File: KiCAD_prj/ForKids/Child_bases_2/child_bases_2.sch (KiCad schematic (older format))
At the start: 61 parts, among them Q1 PN2222A, Q10 PN2222A, Q11 PN2222A, Q2 PN2222A, Q3 PN2222A, Q4 PN2222A, Q5 PN2222A, Q6 2N3904*, Q7 PN2222A, Q8 PN2222A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

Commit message: Update child_babes_2
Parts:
- R8: value 10K -> 47K
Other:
- note removed: "* можно заменить на 2222"
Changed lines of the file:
@@
 P 4650 3700
 F 0 "R8" V 4550 3700 50  0000 C CNN
-F 1 "10K" V 4750 3700 50  0000 C CNN
+F 1 "47K" V 4750 3700 50  0000 C CNN
 F 2 "" V 4580 3700 50  0001 C CNN
 F 3 "~" H 4650 3700 50  0001 C CNN
@@
 	4400 3200 4400 3350
 Connection ~ 4400 3350
-Text Notes 4450 4650 0    50   ~ 0
-* можно заменить на 2222
 $Comp
 L Device:Speaker LS2

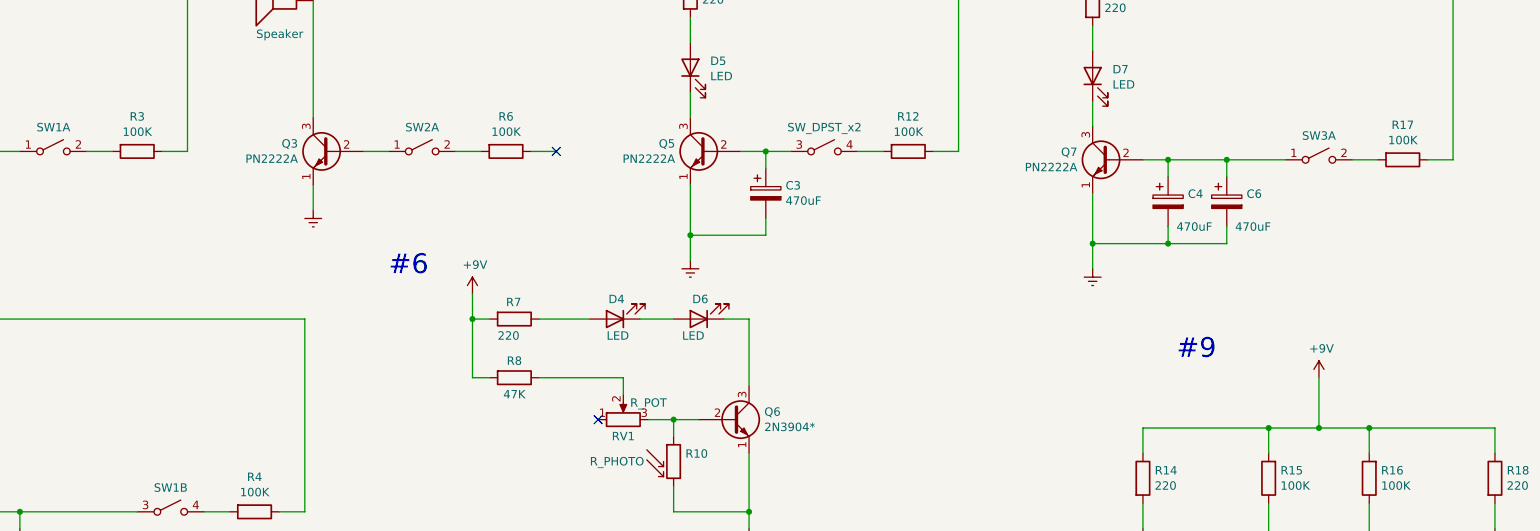
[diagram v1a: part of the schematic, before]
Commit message: Update Child Bases 2 project
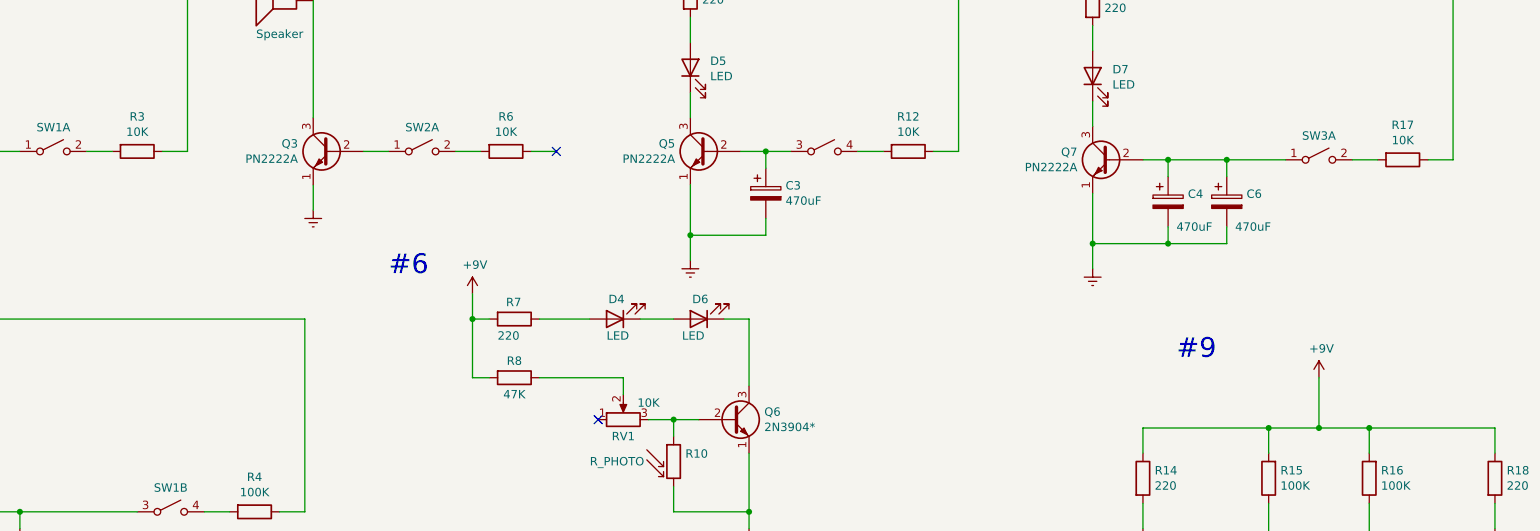
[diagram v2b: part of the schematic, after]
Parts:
- R12, R17, R3, R6: value 100K -> 10K
- RV1: value R_POT -> 10K
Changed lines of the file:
@@
 P 2400 2350
 F 0 "R3" V 2193 2350 50  0000 C CNN
-F 1 "100K" V 2284 2350 50  0000 C CNN
+F 1 "10K" V 2284 2350 50  0000 C CNN
 F 2 "" V 2330 2350 50  0001 C CNN
 F 3 "~" H 2400 2350 50  0001 C CNN
@@
 P 4600 2350
 F 0 "R6" V 4393 2350 50  0000 C CNN
-F 1 "100K" V 4484 2350 50  0000 C CNN
+F 1 "10K" V 4484 2350 50  0000 C CNN
 F 2 "" V 4530 2350 50  0001 C CNN
 F 3 "~" H 4600 2350 50  0001 C CNN
@@
 P 6500 2350
 F 0 "SW2" H 6500 2585 50  0001 C CNN
-F 1 "SW_DPST_x2" H 6500 2493 50  0000 C CNN
+F 1 "SW_DPST_x2" H 6500 2493 50  0001 C CNN
 F 2 "" H 6500 2350 50  0001 C CNN
 F 3 "~" H 6500 2350 50  0001 C CNN
@@
 P 7000 2350
 F 0 "R12" V 6793 2350 50  0000 C CNN
-F 1 "100K" V 6884 2350 50  0000 C CNN
+F 1 "10K" V 6884 2350 50  0000 C CNN
 F 2 "" V 6930 2350 50  0001 C CNN
 F 3 "~" H 7000 2350 50  0001 C CNN
@@
 P 9950 2400
 F 0 "R17" V 9743 2400 50  0000 C CNN
-F 1 "100K" V 9834 2400 50  0000 C CNN
+F 1 "10K" V 9834 2400 50  0000 C CNN
 F 2 "" V 9880 2400 50  0001 C CNN
 F 3 "~" H 9950 2400 50  0001 C CNN
@@
 P 5300 3950
 F 0 "RV1" V 5200 3950 50  0000 C CNN
-F 1 "R_POT" V 5400 3800 50  0000 C CNN
+F 1 "10K" V 5400 3800 50  0000 C CNN
 F 2 "" H 5300 3950 50  0001 C CNN
 F 3 "~" H 5300 3950 50  0001 C CNN

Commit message: Update KiCad child bases 2 project
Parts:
- R15, R16, R4: value 100K -> 10K
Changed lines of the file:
@@
 P 3100 4500
 F 0 "R4" V 2893 4500 50  0000 C CNN
-F 1 "100K" V 2984 4500 50  0000 C CNN
+F 1 "10K" V 2984 4500 50  0000 C CNN
 F 2 "" V 3030 4500 50  0001 C CNN
 F 3 "~" H 3100 4500 50  0001 C CNN
@@
 P 9150 4300
 F 0 "R15" H 9080 4254 50  0000 R CNN
-F 1 "100K" H 9080 4345 50  0000 R CNN
+F 1 "10K" H 9080 4345 50  0000 R CNN
 F 2 "" V 9080 4300 50  0001 C CNN
 F 3 "~" H 9150 4300 50  0001 C CNN
@@
 P 9750 4300
 F 0 "R16" H 9680 4254 50  0000 R CNN
-F 1 "100K" H 9680 4345 50  0000 R CNN
+F 1 "10K" H 9680 4345 50  0000 R CNN
 F 2 "" V 9680 4300 50  0001 C CNN
 F 3 "~" H 9750 4300 50  0001 C CNN
@@
 Text Notes 2700 5100 0    118  ~ 0
 #7
-Text Notes 8600 3600 0    118  ~ 0
+Text Notes 8450 6400 0    118  ~ 0
 #9
 Text Notes 1400 7400 0    118  ~ 0

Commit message: Update Child bases2 project
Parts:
- removed unit 1 of SW2
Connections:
- net at Q3.2 (B): now also R6.2
- no-connect marks 5 -> 3
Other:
- moved on the sheet: LS1
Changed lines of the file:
@@
 L Device:Speaker LS1
 U 1 1 5F978E6E
-P 3250 1350
-F 0 "LS1" H 3300 1550 50  0000 C CNN
-F 1 "Speaker" H 3250 1050 50  0000 C CNN
-F 2 "" H 3250 1150 50  0001 C CNN
-F 3 "~" H 3240 1300 50  0001 C CNN
-	1    3250 1350
+P 3250 1700
+F 0 "LS1" H 3300 1900 50  0000 C CNN
+F 1 "Speaker" H 3250 1400 50  0000 C CNN
+F 2 "" H 3250 1500 50  0001 C CNN
+F 3 "~" H 3240 1650 50  0001 C CNN
+	1    3250 1700
 	-1   0    0    -1
-$EndComp
-$Comp
-L Switch:SW_DPST_x2 SW2
-U 1 1 5F97A5C2
-P 4100 2350
-F 0 "SW2" H 4100 2493 50  0000 C CNN
-F 1 "SW_DPST_x2" H 4100 2494 50  0001 C CNN
-F 2 "" H 4100 2350 50  0001 C CNN
-F 3 "~" H 4100 2350 50  0001 C CNN
-	1    4100 2350
-	1    0    0    -1
 $EndComp
 $Comp
@@
 	3450 2700 3450 2550
 Wire Wire Line
-	3750 2350 3900 2350
-Wire Wire Line
-	4300 2350 4450 2350
-Wire Wire Line
 	4900 2350 4750 2350
-Wire Wire Line
-	3450 1450 3450 2150
 $Comp
 L power:+9V #PWR05
@@
 	1    0    0    -1
 $EndComp
-Wire Wire Line
-	2800 7000 2800 7150
-Wire Wire Line
-	2200 6800 2200 7150
-Connection ~ 2200 6800
-NoConn ~ 2200 7150
-Wire Wire Line
-	2800 7150 2550 7150
-Connection ~ 2800 7150
-Wire Wire Line
-	2800 7150 2800 7350
-NoConn ~ 2550 7150
 Text Notes 850  900  0    118  ~ 0
 #1
@@
 	3450 1250 4900 1250
 Connection ~ 3450 1250
-Wire Wire Line
-	3450 1250 3450 1350
 NoConn ~ 4900 1250
 $Comp
@@
 Wire Wire Line
 	5950 6700 5800 6700
+Wire Wire Line
+	3750 2350 4450 2350
+Wire Wire Line
+	3450 1250 3450 1700
+Wire Wire Line
+	3450 1800 3450 2150
+Wire Wire Line
+	2800 7000 2800 7350
+Wire Notes Line
+	2200 6800 2200 7150
+Wire Notes Line
+	2200 7150 2800 7150
 $EndSCHEMATC

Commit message: Update Child bases2  chem project
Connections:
- net +9V: now also R6.1
- net at LS1.2: no longer Q3.3 (C)
- no-connect marks 3 -> 1
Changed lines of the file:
@@
 	1250 1200 1250 1250
-$Comp
-L Device:Speaker LS1
-U 1 1 5F978E6E
-P 3250 1700
-F 0 "LS1" H 3300 1900 50  0000 C CNN
-F 1 "Speaker" H 3250 1400 50  0000 C CNN
-F 2 "" H 3250 1500 50  0001 C CNN
-F 3 "~" H 3240 1650 50  0001 C CNN
-	1    3250 1700
-	-1   0    0    -1
-$EndComp
 $Comp
 L Transistor_BJT:PN2222A Q3
@@
 	1    0    0    -1
 $EndComp
-NoConn ~ 4900 2350
 $Comp
 L Switch:SW_DPST_x2 SW2
@@
 Wire Wire Line
 	3450 1250 4900 1250
-Connection ~ 3450 1250
-NoConn ~ 4900 1250
 $Comp
 L Transistor_BJT:PN2222A Q10
@@
 	3750 2350 4450 2350
 Wire Wire Line
-	3450 1250 3450 1700
-Wire Wire Line
-	3450 1800 3450 2150
-Wire Wire Line
 	2800 7000 2800 7350
 Wire Notes Line
@@
 Wire Notes Line
 	2200 7150 2800 7150
+Wire Wire Line
+	4900 2350 4900 1250
+Connection ~ 3450 1250
+Wire Wire Line
+	3450 1700 3450 1250
+$Comp
+L Device:Speaker LS1
+U 1 1 5F978E6E
+P 3250 1700
+F 0 "LS1" H 3300 1900 50  0000 C CNN
+F 1 "Speaker" H 3250 1400 50  0000 C CNN
+F 2 "" H 3250 1500 50  0001 C CNN
+F 3 "~" H 3240 1650 50  0001 C CNN
+	1    3250 1700
+	-1   0    0    -1
+$EndComp
+Wire Wire Line
+	3450 1800 3800 1800
+Wire Wire Line
+	3450 2150 3450 2050
+Wire Wire Line
+	3450 2050 3800 2050
+Wire Notes Line
+	3800 1800 3800 2050
 $EndSCHEMATC
